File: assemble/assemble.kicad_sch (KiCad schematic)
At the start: 94 parts, among them J1 Conn_01x04, SW1 SW_Push, SW10 SW_Push, SW11 SW_Push, SW12 SW_Push, SW13 SW_Push, SW14 SW_Push, SW15 SW_Push, SW16 SW_Push, SW17 SW_Push, SW18 SW_Push, SW19 SW_Push, SW2 SW_Push, SW20 SW_Push, SW21 SW_Push, SW22 SW_Push, SW23 SW_Push, SW24 SW_Push, SW25 SW_Push, SW26 SW_Push, SW27 SW_Push, SW28 SW_Push, SW29 SW_Push, SW3 SW_Push, SW30 SW_Push, SW31 SW_Push, SW32 SW_Push, SW33 SW_Push, SW34 SW_Push, SW35 SW_Push, SW36 SW_Push, SW37 SW_Push, SW38 SW_Push, SW39 SW_Push, SW4 SW_Push, SW40 SW_Push, SW41 SW_Push, SW42 SW_Push, SW45 RotaryEncoder_Switch, SW46 RotaryEncoder_Switch, SW47 SW_SPDT, SW5 SW_Push, SW6 SW_Push, SW7 SW_Push, SW8 SW_Push, SW9 SW_Push, U1 XIAO-nRF52840-SMD, U4 XIAO-nRF52840-SMD

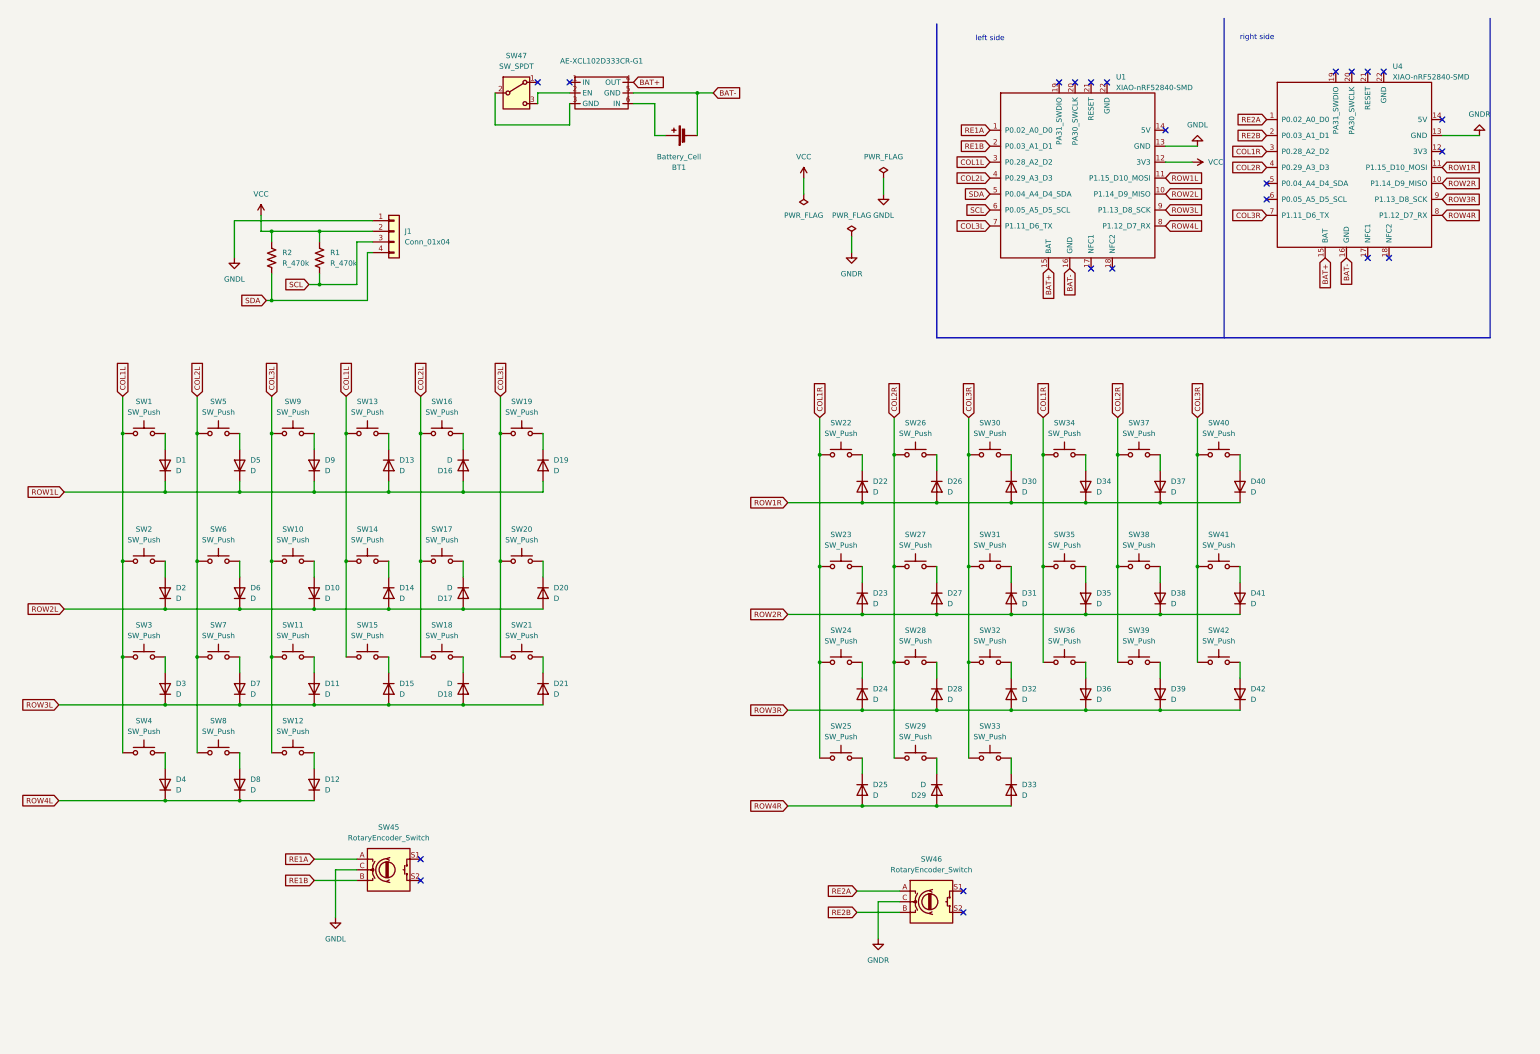
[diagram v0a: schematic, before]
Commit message: feat: implement schematic and PCB partially
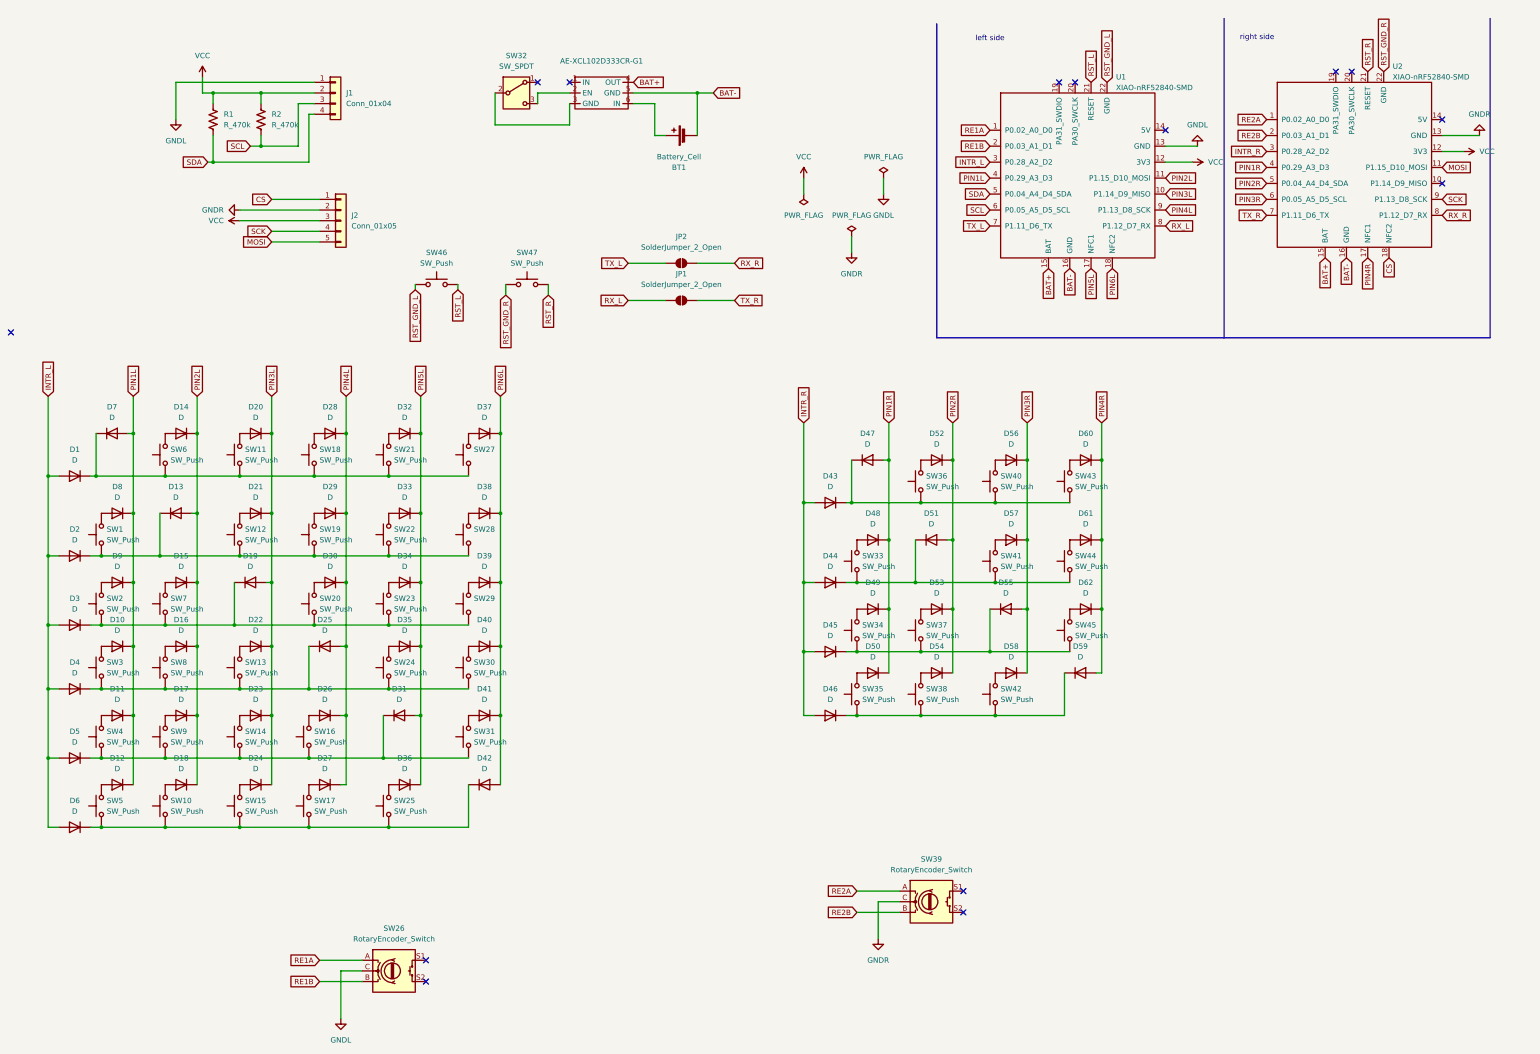
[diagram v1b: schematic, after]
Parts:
- removed SW26, SW32, SW39: SW_Push, kicad-lib:CherryMX-HotSwap-1u_17, symbol Switch:SW_Push
- added D43, D44, D45, D46, D47, D48, D49, D50, D51, D52, D53, D54, D55, D56, D57, D58, D59, D60, D61, D62: D, kbd_Parts:Diode_SMD, symbol Device:D
- added J2: Conn_01x05, Connector_PinHeader_1.00mm:PinHeader_1x05_P1.00mm_Vertical, symbol Connector_Generic:Conn_01x05
- added JP1, JP2: SolderJumper_2_Open, Jumper:SolderJumper-2_P1.3mm_Open_Pad1.0x1.5mm, symbol Jumper:SolderJumper_2_Open
- added SW43, SW44, SW45: SW_Push, kicad-lib:Choc_v2_Hotswap_1u_16.6, symbol Switch:SW_Push
- added SW46, SW47: SW_Push, kbd_Parts:ResetSW, symbol Switch:SW_Push
- BT1: footprint kbd_Parts:Battery_AAA -> Battery:BatteryHolder_Keystone_2460_1xAA
- SW1, SW10, SW11, SW12, SW13, SW14, SW15, SW16, SW17, SW18, SW19, SW2, SW20, SW21, SW22, SW23, SW24, SW25, SW27, SW28, SW29, SW3, SW30, SW31, SW33, SW34, SW35, SW36, SW37, SW38, SW4, SW40, SW41, SW42, SW5, SW6, SW7, SW8, SW9: footprint kicad-lib:CherryMX-HotSwap-1u_17 -> kicad-lib:Choc_v2_Hotswap_1u_16.6
- renumbered R2 to R1, R1 to R2, SW45 to SW26, SW47 to SW32, SW46 to SW39, U4 to U2
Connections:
- net GNDR: now also J2.2 (Pin_2)
- net VCC: now also U2.12 (3V3), J2.3 (Pin_3)
- net PIN5L: now reaches U1.17 (NFC1)
- net PIN5L: now also D31.2 (A), D32.1 (K), D33.1 (K), D34.1 (K), D35.1 (K), D36.1 (K)
- net PIN6L: now reaches U1.18 (NFC2)
- net PIN6L: now also D37.1 (K), D38.1 (K), D39.1 (K), D40.1 (K), D41.1 (K), D42.2 (A)
- net RST_L: now reaches U1.21 (RESET)
- net RST_L: now also SW46.2
- net RST_GND_L: now reaches U1.22 (GND)
- net RST_GND_L: now also SW46.1
- net at SW35.2: now also D50.2 (A); no longer D35.2 (A)
- net at SW37.2: now also D53.2 (A); no longer D37.2 (A)
- net at SW22.2: now also D33.2 (A); no longer D22.1 (K)
- net at SW17.2: now also D27.2 (A); no longer D17.1 (K)
- net at SW9.2: now also D17.2 (A); no longer D9.2 (A)
- net at D25.1 (K): now also D4.1 (K), SW13.1, SW24.1, SW3.1, SW30.1, SW8.1; no longer SW25.2
- net at SW4.2: now also D11.2 (A); no longer D4.2 (A)
- net at D34.2 (A): now also SW23.2; no longer SW34.2
- net at SW29.2: now also D39.2 (A); no longer D29.1 (K)
- net at SW36.2: now also D52.2 (A); no longer D36.2 (A)
- net at SW27.2: now also D37.2 (A); no longer D27.1 (K)
- net PIN4L: now reaches D26.1 (K)
- net PIN4L: now also D25.2 (A), D27.1 (K), D28.1 (K), D29.1 (K), D30.1 (K), U1.9 (P1.13_D8_SCK)
- net at SW2.2: now also D9.2 (A); no longer D2.2 (A)
- net PIN3L: now reaches D23.1 (K)
- net PIN3L: now also D19.2 (A), D20.1 (K), D21.1 (K), D22.1 (K), D24.1 (K), U1.10 (P1.14_D9_MISO); no longer SW23.2
- net at SW5.2: now also D12.2 (A); no longer D5.2 (A)
- net at D10.2 (A): now also SW3.2; no longer SW10.2
- net at D19.1 (K): now also D3.1 (K), SW2.1, SW20.1, SW23.1, SW29.1, SW7.1; no longer SW19.2
- net at SW42.2: now also D58.2 (A); no longer D42.2 (A)
- net at SW15.2: now also D24.2 (A); no longer D15.1 (K)
- net at SW1.2: now also D8.2 (A); no longer D1.2 (A)
- net INTR_L: now reaches D3.2 (A)
- net INTR_L: now also D1.2 (A), D2.2 (A), D4.2 (A), D5.2 (A), D6.2 (A), U1.3 (P0.28_A2_D2); no longer SW3.2
- net at SW18.2: now also D28.2 (A); no longer D18.1 (K)
- net at SW7.2: now also D15.2 (A); no longer D7.2 (A)
- net at D13.1 (K): now also D2.1 (K), SW1.1, SW12.1, SW19.1, SW22.1, SW28.1; no longer SW13.2
- net at SW33.2: now also D48.2 (A); no longer D33.1 (K)
- net at SW20.2: now also D30.2 (A); no longer D20.1 (K)
- net at SW21.2: now also D32.2 (A); no longer D21.1 (K)
- net at SW6.2: now also D14.2 (A); no longer D6.2 (A)
- net at SW16.2: now also D26.2 (A); no longer D16.1 (K)
- net at D38.2 (A): now also SW28.2; no longer SW38.2
- net at SW40.2: now also D56.2 (A); no longer D40.2 (A)
- net at SW30.2: now also D40.2 (A); no longer D30.1 (K)
- net at SW24.2: now also D35.2 (A); no longer D24.1 (K)
- net PIN4R: now reaches U2.17 (NFC1)
- net PIN4R: now also D59.2 (A), D60.1 (K), D61.1 (K), D62.1 (K)
- net CS: now reaches U2.18 (NFC2)
- net CS: now also J2.1 (Pin_1)
- net RST_R: now reaches U2.21 (RESET)
- net RST_R: now also SW47.2
- net RST_GND_R: now reaches U2.22 (GND)
- net RST_GND_R: now also SW47.1
- net PIN2R: now reaches U2.5 (P0.04_A4_D4_SDA)
- net PIN2R: now also D51.2 (A), D52.1 (K), D53.1 (K), D54.1 (K)
- net PIN3R: now reaches U2.6 (P0.05_A5_D5_SCL)
- net PIN3R: now also D55.2 (A), D56.1 (K), D57.1 (K), D58.1 (K)
- net at D41.2 (A): now also SW31.2; no longer SW41.2
- net at SW14.2: now also D23.2 (A); no longer D14.1 (K)
- net at SW12.2: now also D21.2 (A); no longer D12.2 (A)
- net at SW11.2: now also D20.2 (A); no longer D11.2 (A)
- net at SW8.2: now also D16.2 (A); no longer D8.2 (A)
- net at D31.1 (K): now also D5.1 (K), SW14.1, SW16.1, SW31.1, SW4.1, SW9.1; no longer SW31.2
- removed net COL1L: SW1.1, SW13.1, SW14.1, SW15.1, SW2.1, SW3.1, SW4.1, U1.3 (P0.28_A2_D2)
- removed net COL1R: SW22.1, SW23.1, SW24.1, SW25.1, SW34.1, SW35.1, SW36.1, U2.3 (P0.28_A2_D2)
- removed net COL2L: SW16.1, SW17.1, SW18.1, SW5.1, SW6.1, SW7.1, SW8.1, U1.4 (P0.29_A3_D3)
- removed net COL2R: SW27.1, SW28.1, SW29.1, SW37.1, SW38.1, U2.4 (P0.29_A3_D3)
- removed net COL3L: SW10.1, SW11.1, SW12.1, SW19.1, SW20.1, SW21.1, SW9.1, U1.7 (P1.11_D6_TX)
- removed net COL3R: SW30.1, SW31.1, SW33.1, SW40.1, SW41.1, SW42.1, U2.7 (P1.11_D6_TX)
- removed net ROW1L: D1.1 (K), D13.2 (A), D16.2 (A), D19.2 (A), D5.1 (K), D9.1 (K), U1.11 (P1.15_D10_MOSI)
- removed net ROW1R: D22.2 (A), D26.2 (A), D30.2 (A), D34.1 (K), D37.1 (K), D40.1 (K), U2.11 (P1.15_D10_MOSI)
- removed net ROW2L: D10.1 (K), D14.2 (A), D17.2 (A), D2.1 (K), D20.2 (A), D6.1 (K), U1.10 (P1.14_D9_MISO)
- removed net ROW2R: D23.2 (A), D27.2 (A), D31.2 (A), D35.1 (K), D38.1 (K), D41.1 (K), U2.10 (P1.14_D9_MISO)
- removed net ROW3L: D11.1 (K), D15.2 (A), D18.2 (A), D21.2 (A), D3.1 (K), D7.1 (K), U1.9 (P1.13_D8_SCK)
- removed net ROW3R: D24.2 (A), D28.2 (A), D32.2 (A), D36.1 (K), D39.1 (K), D42.1 (K), U2.9 (P1.13_D8_SCK)
- net ROW4L renamed PIN1L
- net PIN1L: now also D10.1 (K), D11.1 (K), D7.2 (A), D9.1 (K), U1.4 (P0.29_A3_D3); no longer D4.1 (K), U1.8 (P1.12_D7_RX)
- removed net ROW4R: D25.2 (A), D29.2 (A), D33.2 (A), U2.8 (P1.12_D7_RX)
- new net: D44.1 (K), D51.1 (K), SW33.1, SW41.1, SW44.1
- new net: D57.2 (A), SW41.2
- new net: D46.1 (K), D59.1 (K), SW35.1, SW38.1, SW42.1
- new net: D1.1 (K), D7.1 (K), SW11.1, SW18.1, SW21.1, SW27.1, SW6.1
- new net: D43.1 (K), D47.1 (K), SW36.1, SW40.1, SW43.1
- new net: D60.2 (A), SW43.2
- new net: D62.2 (A), SW45.2
- new net: D42.1 (K), D6.1 (K), SW10.1, SW15.1, SW17.1, SW25.1, SW5.1
- new net: D54.2 (A), SW38.2
- new net: D18.2 (A), SW10.2
- new net: D61.2 (A), SW44.2
- new net: D29.2 (A), SW19.2
- new net: D45.1 (K), D55.1 (K), SW34.1, SW37.1, SW45.1
- new net: D36.2 (A), SW25.2
- new net: D49.2 (A), SW34.2
- new net: D22.2 (A), SW13.2
- new net INTR_R: D43.2 (A), D44.2 (A), D45.2 (A), D46.2 (A), U2.3 (P0.28_A2_D2)
- new net MOSI: J2.5 (Pin_5), U2.11 (P1.15_D10_MOSI)
- new net PIN1R: D47.2 (A), D48.1 (K), D49.1 (K), D50.1 (K), U2.4 (P0.29_A3_D3)
- new net PIN2L: D13.2 (A), D14.1 (K), D15.1 (K), D16.1 (K), D17.1 (K), D18.1 (K), U1.11 (P1.15_D10_MOSI)
- new net RX_L: JP1.1 (A), U1.8 (P1.12_D7_RX)
- new net RX_R: JP2.2 (B), U2.8 (P1.12_D7_RX)
- new net SCK: J2.4 (Pin_4), U2.9 (P1.13_D8_SCK)
- new net TX_L: JP2.1 (A), U1.7 (P1.11_D6_TX)
- new net TX_R: JP1.2 (B), U2.7 (P1.11_D6_TX)
- no-connect marks 23 -> 14
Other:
- moved on the sheet: J1, R1, R2, SW26

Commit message: feat: implement some features
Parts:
- J2: footprint Connector_PinHeader_1.00mm:PinHeader_1x05_P1.00mm_Vertical -> Connector_PinHeader_2.00mm:PinHeader_1x05_P2.00mm_Vertical
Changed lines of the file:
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@@
 			)
 		)
-		(property "Footprint" "Connector_PinHeader_1.00mm:PinHeader_1x05_P1.00mm_Vertical"
+		(property "Footprint" "Connector_PinHeader_2.00mm:PinHeader_1x05_P2.00mm_Vertical"
 			(at 113.03 60.96 0)
 			(effects

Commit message: feat: implement PCB
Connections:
- net VCC renamed VCCL
- net VCCL: no longer J2.3 (Pin_3), U2.12 (3V3)
- new net VCCR: J2.3 (Pin_3), U2.12 (3V3)
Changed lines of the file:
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@@
 	(wire
 		(pts
+			(xy 212.09 54.61) (xy 212.09 50.8)
+		)
+		(stroke
+			(width 0)
+			(type default)
+		)
+	)
+	(wire
+		(pts
 			(xy 54.61 121.92) (xy 71.12 121.92)
 		)
@@
 			)
 		)
-		(property "Value" "VCC"
-			(at 85.09 60.9599 90)
+		(property "Value" "VCCR"
+			(at 87.63 58.42 90)
 			(effects
 				(font
 					(size 1.27 1.27)
 				)
-				(justify left)
 			)
 		)
@@
 	)
 	(symbol
+		(lib_id "power:VCC")
+		(at 212.09 50.8 0)
+		(unit 1)
+		(exclude_from_sim no)
+		(in_bom yes)
+		(on_board yes)
+		(dnp no)
+		(fields_autoplaced yes)
+		(property "Reference" "#PWR014"
+			(at 212.09 54.61 0)
+			(effects
+				(font
+					(size 1.27 1.27)
+				)
+				(hide yes)
+			)
+		)
+		(property "Value" "VCCL"
+			(at 212.09 45.72 0)
+			(effects
+				(font
+					(size 1.27 1.27)
+				)
+			)
+		)
+		(property "Footprint" ""
+			(at 212.09 50.8 0)
+			(effects
+				(font
+					(size 1.27 1.27)
+				)
+				(hide yes)
+			)
+		)
+		(property "Datasheet" ""
+			(at 212.09 50.8 0)
+			(effects
+				(font
+					(size 1.27 1.27)
+				)
+				(hide yes)
+			)
+		)
+		(property "Description" "Power symbol creates a global label with name \"VCC\""
+			(at 212.09 50.8 0)
+			(effects
+				(font
+					(size 1.27 1.27)
+				)
+				(hide yes)
+			)
+		)
+		(pin "1"
+		)
+		(instances
+			(project "assemble"
+				(path "/3bde1348-5ac1-4130-8742-e5aed0e7aea9"
+					(reference "#PWR014")
+					(unit 1)
+				)
+			)
+		)
+	)
+	(symbol
 		(lib_id "Device:D")
 		(at 92.71 195.58 180)
@@
 			)
 		)
-		(property "Value" "VCC"
-			(at 80.01 21.59 0)
+		(property "Value" "VCCL"
+			(at 82.55 25.3999 0)
 			(effects
 				(font
 					(size 1.27 1.27)
 				)
+				(justify left)
 			)
 		)
@@
 			)
 		)
-		(property "Value" "VCC"
-			(at 223.52 45.72 0)
+		(property "Value" "VCCR"
+			(at 226.06 49.5299 0)
 			(effects
 				(font
 					(size 1.27 1.27)
 				)
+				(justify left)
 			)
 		)
@@
 			)
 		)
-		(property "Value" "VCC"
+		(property "Value" "VCCL"
 			(at 320.04 46.9899 90)
 			(effects
@@
 	)
 	(symbol
+		(lib_id "power:PWR_FLAG")
+		(at 212.09 54.61 180)
+		(unit 1)
+		(exclude_from_sim no)
+		(in_bom yes)
+		(on_board yes)
+		(dnp no)
+		(fields_autoplaced yes)
+		(property "Reference" "#FLG04"
+			(at 212.09 56.515 0)
+			(effects
+				(font
+					(size 1.27 1.27)
+				)
+				(hide yes)
+			)
+		)
+		(property "Value" "PWR_FLAG"
+			(at 212.09 59.69 0)
+			(effects
+				(font
+					(size 1.27 1.27)
+				)
+			)
+		)
+		(property "Footprint" ""
+			(at 212.09 54.61 0)
+			(effects
+				(font
+					(size 1.27 1.27)
+				)
+				(hide yes)
+			)
+		)
+		(property "Datasheet" "~"
+			(at 212.09 54.61 0)
+			(effects
+				(font
+					(size 1.27 1.27)
+				)
+				(hide yes)
+			)
+		)
+		(property "Description" "Special symbol for telling ERC where power comes from"
+			(at 212.09 54.61 0)
+			(effects
+				(font
+					(size 1.27 1.27)
+				)
+				(hide yes)
+			)
+		)
+		(pin "1"
+		)
+		(instances
+			(project "assemble"
+				(path "/3bde1348-5ac1-4130-8742-e5aed0e7aea9"
+					(reference "#FLG04")
+					(unit 1)
+				)
+			)
+		)
+	)
+	(symbol
 		(lib_id "Device:D")
 		(at 240.03 153.67 180)
@@
 			)
 		)
-		(property "Value" "VCC"
+		(property "Value" "VCCR"
 			(at 384.81 44.4499 90)
 			(effects

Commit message: feat: PCB renewal
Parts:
- J2: footprint Connector_PinHeader_2.00mm:PinHeader_1x05_P2.00mm_Vertical -> Connector_PinHeader_2.54mm:PinHeader_1x05_P2.54mm_Vertical
- renumbered JP2 to JP1, JP1 to JP2, SW27 to SW26, SW28 to SW27, SW29 to SW28, SW30 to SW29, SW31 to SW30, SW33 to SW31, SW34 to SW32, SW35 to SW33, SW36 to SW34, SW37 to SW35, SW38 to SW36, SW40 to SW37, SW41 to SW38, SW42 to SW39, SW43 to SW40, SW44 to SW41, SW45 to SW42, SW26 to SW43, SW32 to SW44, SW46 to SW45, SW39 to SW46
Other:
- moved on the sheet: AE-XCL102D333CR-G1, BT1, SW43, SW44, SW45, SW46, SW47
